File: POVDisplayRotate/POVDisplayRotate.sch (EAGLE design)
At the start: 34 parts, among them IC1 317EMP

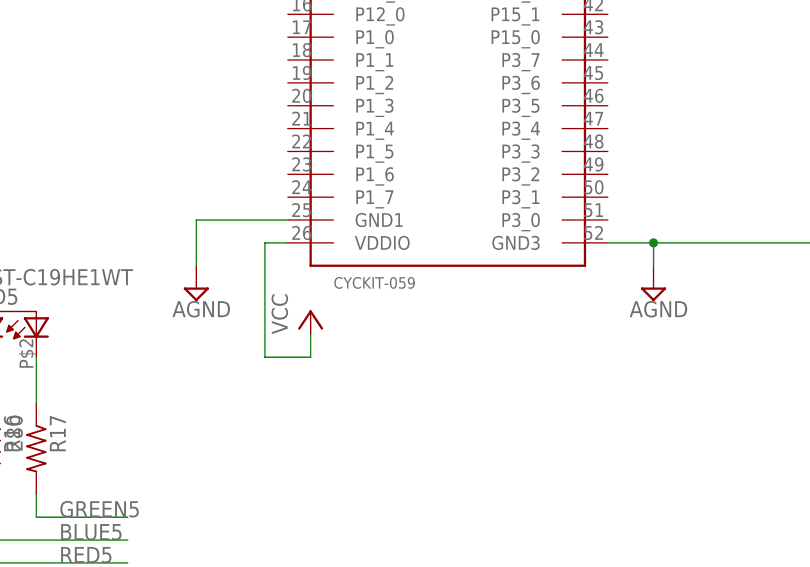
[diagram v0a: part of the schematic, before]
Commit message: Update the POVDisplayRotate.
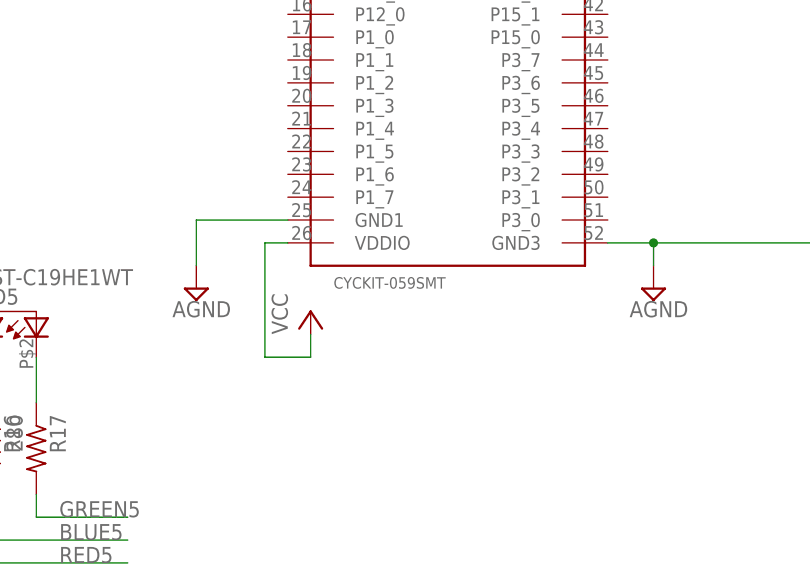
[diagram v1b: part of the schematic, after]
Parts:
- D2: DIGIKEY (none) -> 365-1908-1-ND
- U$1: value CYCKIT-059 -> CYCKIT-059SMT; device NicksParts:CYCKIT-059 -> NicksParts:CYCKIT-059SMT
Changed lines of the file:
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@@
 <grid distance="0.1" unitdist="inch" unit="inch" style="lines" multiple="1" display="no" altdistance="0.01" altunitdist="inch" altunit="inch"/>
 <layers>
-<layer number="1" name="Top" color="4" fill="1" visible="no" active="no"/>
-<layer number="16" name="Bottom" color="1" fill="1" visible="no" active="no"/>
-<layer number="17" name="Pads" color="2" fill="1" visible="no" active="no"/>
-<layer number="18" name="Vias" color="2" fill="1" visible="no" active="no"/>
-<layer number="19" name="Unrouted" color="6" fill="1" visible="no" active="no"/>
-<layer number="20" name="Dimension" color="15" fill="1" visible="no" active="no"/>
-<layer number="21" name="tPlace" color="7" fill="1" visible="no" active="no"/>
-<layer number="22" name="bPlace" color="7" fill="1" visible="no" active="no"/>
-<layer number="23" name="tOrigins" color="15" fill="1" visible="no" active="no"/>
-<layer number="24" name="bOrigins" color="15" fill="1" visible="no" active="no"/>
-<layer number="25" name="tNames" color="7" fill="1" visible="no" active="no"/>
-<layer number="26" name="bNames" color="7" fill="1" visible="no" active="no"/>
-<layer number="27" name="tValues" color="7" fill="1" visible="no" active="no"/>
-<layer number="28" name="bValues" color="7" fill="1" visible="no" active="no"/>
+<layer number="1" name="Top" color="4" fill="1" visible="yes" active="no"/>
+<layer number="16" name="Bottom" color="1" fill="1" visible="yes" active="no"/>
+<layer number="17" name="Pads" color="2" fill="1" visible="yes" active="no"/>
+<layer number="18" name="Vias" color="2" fill="1" visible="yes" active="no"/>
+<layer number="19" name="Unrouted" color="6" fill="1" visible="yes" active="no"/>
+<layer number="20" name="Dimension" color="15" fill="1" visible="yes" active="no"/>
+<layer number="21" name="tPlace" color="16" fill="1" visible="yes" active="no"/>
+<layer number="22" name="bPlace" color="14" fill="1" visible="yes" active="no"/>
+<layer number="23" name="tOrigins" color="15" fill="1" visible="yes" active="no"/>
+<layer number="24" name="bOrigins" color="15" fill="1" visible="yes" active="no"/>
+<layer number="25" name="tNames" color="7" fill="1" visible="yes" active="no"/>
+<layer number="26" name="bNames" color="7" fill="1" visible="yes" active="no"/>
+<layer number="27" name="tValues" color="7" fill="1" visible="yes" active="no"/>
+<layer number="28" name="bValues" color="7" fill="1" visible="yes" active="no"/>
 <layer number="29" name="tStop" color="7" fill="3" visible="no" active="no"/>
 <layer number="30" name="bStop" color="7" fill="6" visible="no" active="no"/>
@@
 <layer number="35" name="tGlue" color="7" fill="4" visible="no" active="no"/>
 <layer number="36" name="bGlue" color="7" fill="5" visible="no" active="no"/>
-<layer number="37" name="tTest" color="7" fill="1" visible="no" active="no"/>
-<layer number="38" name="bTest" color="7" fill="1" visible="no" active="no"/>
+<layer number="37" name="tTest" color="7" fill="1" visible="yes" active="no"/>
+<layer number="38" name="bTest" color="7" fill="1" visible="yes" active="no"/>
 <layer number="39" name="tKeepout" color="4" fill="11" visible="no" active="no"/>
 <layer number="40" name="bKeepout" color="1" fill="11" visible="no" active="no"/>
@@
 <layer number="44" name="Drills" color="7" fill="1" visible="no" active="no"/>
 <layer number="45" name="Holes" color="7" fill="1" visible="no" active="no"/>
-<layer number="46" name="Milling" color="3" fill="1" visible="no" active="no"/>
-<layer number="47" name="Measures" color="7" fill="1" visible="no" active="no"/>
-<layer number="48" name="Document" color="7" fill="1" visible="no" active="no"/>
-<layer number="49" name="Reference" color="7" fill="1" visible="no" active="no"/>
-<layer number="51" name="tDocu" color="6" fill="1" visible="no" active="no"/>
-<layer number="52" name="bDocu" color="7" fill="1" visible="no" active="no"/>
+<layer number="46" name="Milling" color="3" fill="1" visible="yes" active="no"/>
+<layer number="47" name="Measures" color="7" fill="1" visible="yes" active="no"/>
+<layer number="48" name="Document" color="7" fill="1" visible="yes" active="no"/>
+<layer number="49" name="Reference" color="7" fill="1" visible="yes" active="no"/>
+<layer number="51" name="tDocu" color="6" fill="1" visible="yes" active="no"/>
+<layer number="52" name="bDocu" color="7" fill="1" visible="yes" active="no"/>
 <layer number="90" name="Modules" color="5" fill="1" visible="yes" active="yes"/>
 <layer number="91" name="Nets" color="2" fill="1" visible="yes" active="yes"/>
@@
 <attribute name="DIGIKEY" value="MMSZ5232B-FDICT-ND"/>
 </part>
-<part name="U$1" library="NicksParts" deviceset="CY*CKIT-059" device=""/>
+<part name="U$1" library="NicksParts" deviceset="CY*CKIT-059" device="SMT" value="CYCKIT-059SMT"/>
 <part name="LED1" library="NicksParts" deviceset="LTST-C19HE1WT" device="">
 <attribute name="DIGIKEY" value="160-2162-1-ND"/>
@@
 <part name="SUPPLY10" library="supply2" deviceset="AGND" device=""/>
 <part name="P+4" library="supply1" deviceset="VCC" device=""/>
-<part name="D2" library="NicksParts" deviceset="OP980" device=""/>
+<part name="D2" library="NicksParts" deviceset="OP980" device="">
+<attribute name="DIGIKEY" value="365-1908-1-ND"/>
+</part>
 <part name="SUPPLY11" library="supply2" deviceset="AGND" device=""/>
 </parts>
@@
 <instance part="SUPPLY10" gate="G$1" x="231.14" y="27.94"/>
 <instance part="P+4" gate="VCC" x="193.04" y="25.4"/>
-<instance part="D2" gate="G$1" x="254" y="73.66"/>
+<instance part="D2" gate="G$1" x="254" y="73.66">
+<attribute name="DIGIKEY" x="254" y="73.66" size="1.778" layer="96" display="off"/>
+</instance>
 <instance part="SUPPLY11" gate="G$1" x="254" y="88.9"/>
 </instances>
@@
 </sheet>
 </sheets>
-<errors>
-</errors>
 </schematic>
 </drawing>

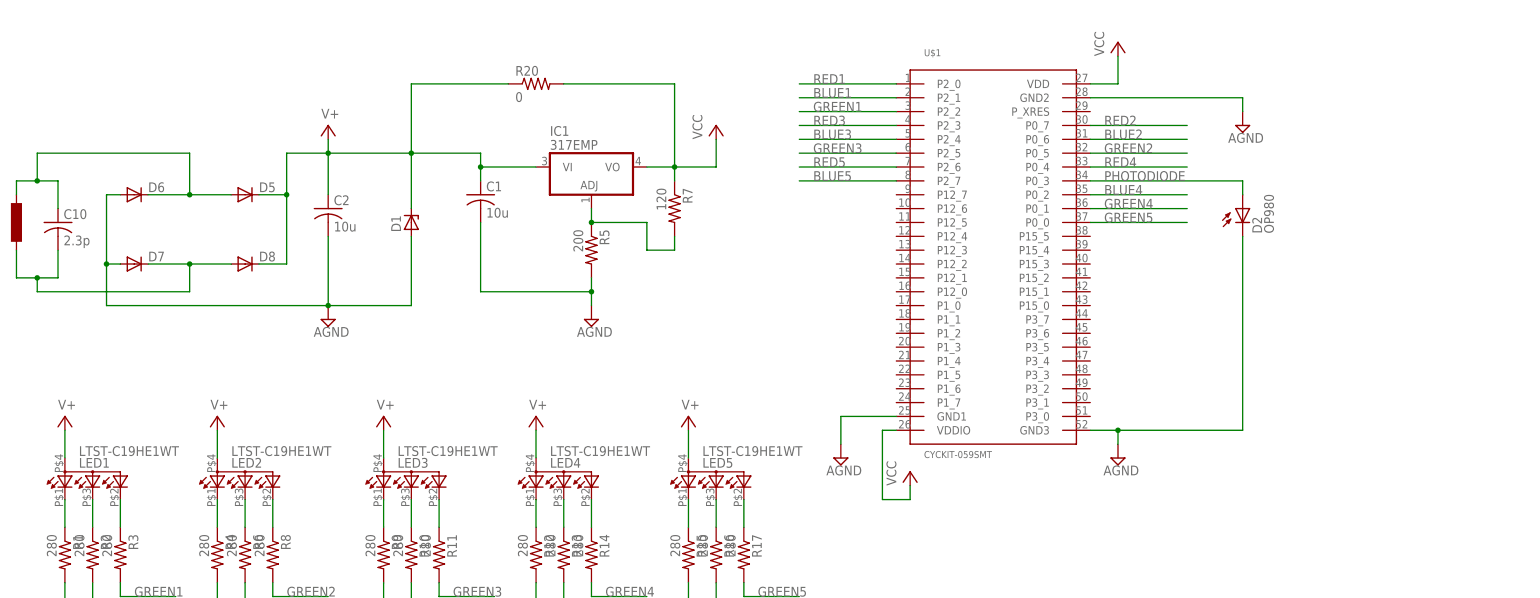
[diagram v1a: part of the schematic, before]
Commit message: Added Abercrombie blockage monitor.
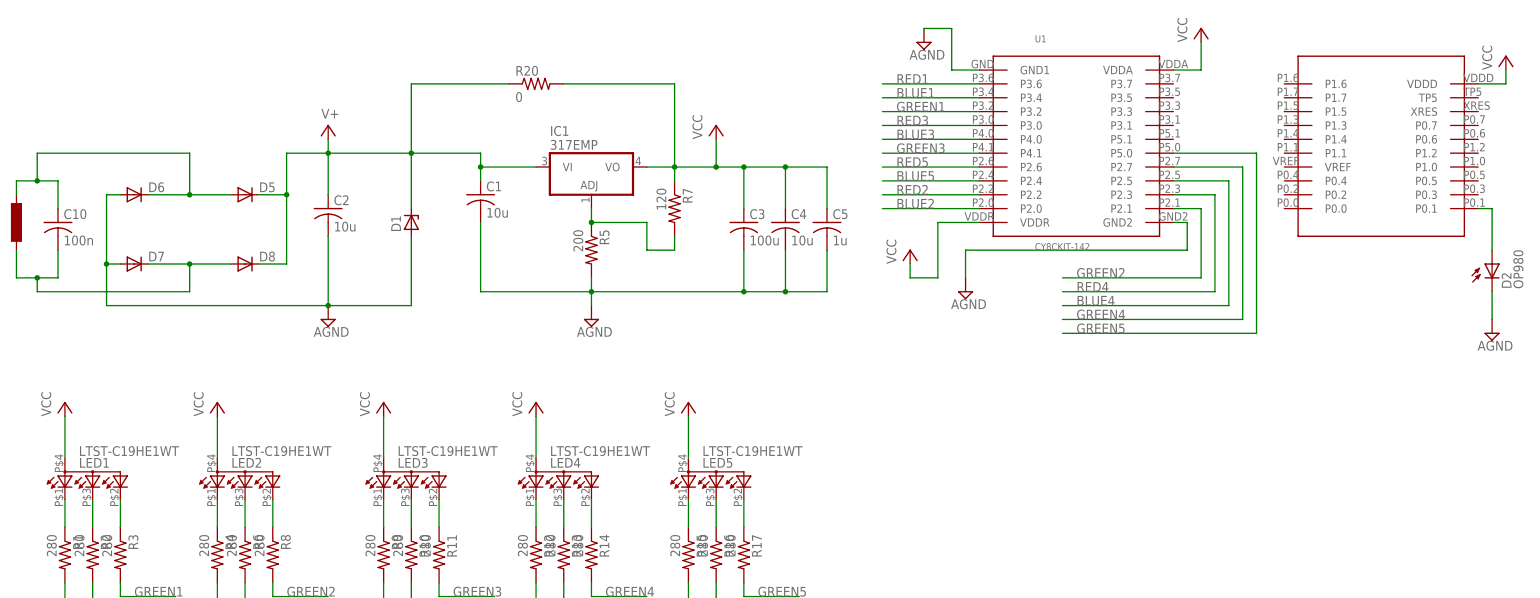
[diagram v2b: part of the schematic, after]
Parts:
- removed U$1: CYCKIT-059SMT, NicksParts:CYCKIT-059SMT
- added C3: 100u, resistor:C-USC0603
- added C4: 10u, resistor:C-USC0603
- added C5: 1u, resistor:C-USC0603
- added U1: CY8CKIT-142, NicksParts:CY8CKIT-142
- C10: value 2.3p -> 100n
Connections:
- net AGND: now also C3.2, C4.2, C5.2, U1.GND1, U1.GND2; no longer U$1.GND1, U$1.GND2, U$1.GND3
- net BLUE1: now also U1.P3.4; no longer U$1.P2_1
- net BLUE2: now also U1.P2.0; no longer U$1.P0_6
- net BLUE3: now also U1.P4.0; no longer U$1.P2_4
- net BLUE4: now also U1.P2.5; no longer U$1.P0_2
- net BLUE5: now also U1.P2.4; no longer U$1.P2_7
- net GREEN1: now also U1.P3.2; no longer U$1.P2_2
- net GREEN2: now also U1.P2.1; no longer U$1.P0_5
- net GREEN3: now also U1.P4.1; no longer U$1.P2_5
- net GREEN4: now also U1.P2.7; no longer U$1.P0_1
- net GREEN5: now also U1.P5.0; no longer U$1.P0_0
- net PHOTODIODE: now also U1.P0.1; no longer U$1.P0_3
- net RED1: now also U1.P3.6; no longer U$1.P2_0
- net RED2: now also U1.P2.2; no longer U$1.P0_7
- net RED3: now also U1.P3.0; no longer U$1.P2_3
- net RED4: now also U1.P2.3; no longer U$1.P0_4
- net RED5: now also U1.P2.6; no longer U$1.P2_6
- net V+: no longer LED1.A, LED2.A, LED3.A, LED4.A, LED5.A
- net VCC: now also C3.1, C4.1, C5.1, LED1.A, LED2.A, LED3.A, LED4.A, LED5.A, U1.VDDA, U1.VDDD, U1.VDDR; no longer U$1.VDD, U$1.VDDIO
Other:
- moved on the sheet: D2

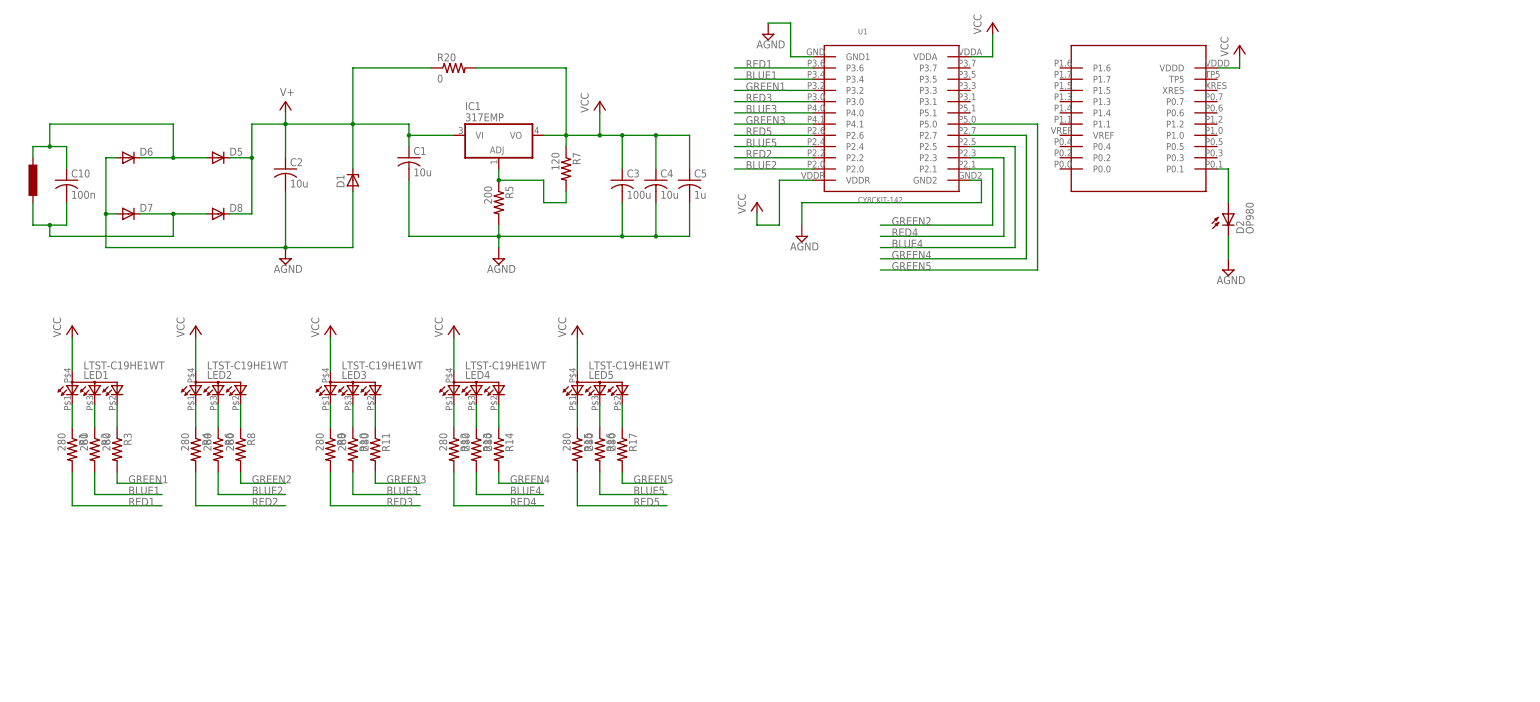
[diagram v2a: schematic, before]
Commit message: Updated the POVDisplayRotate
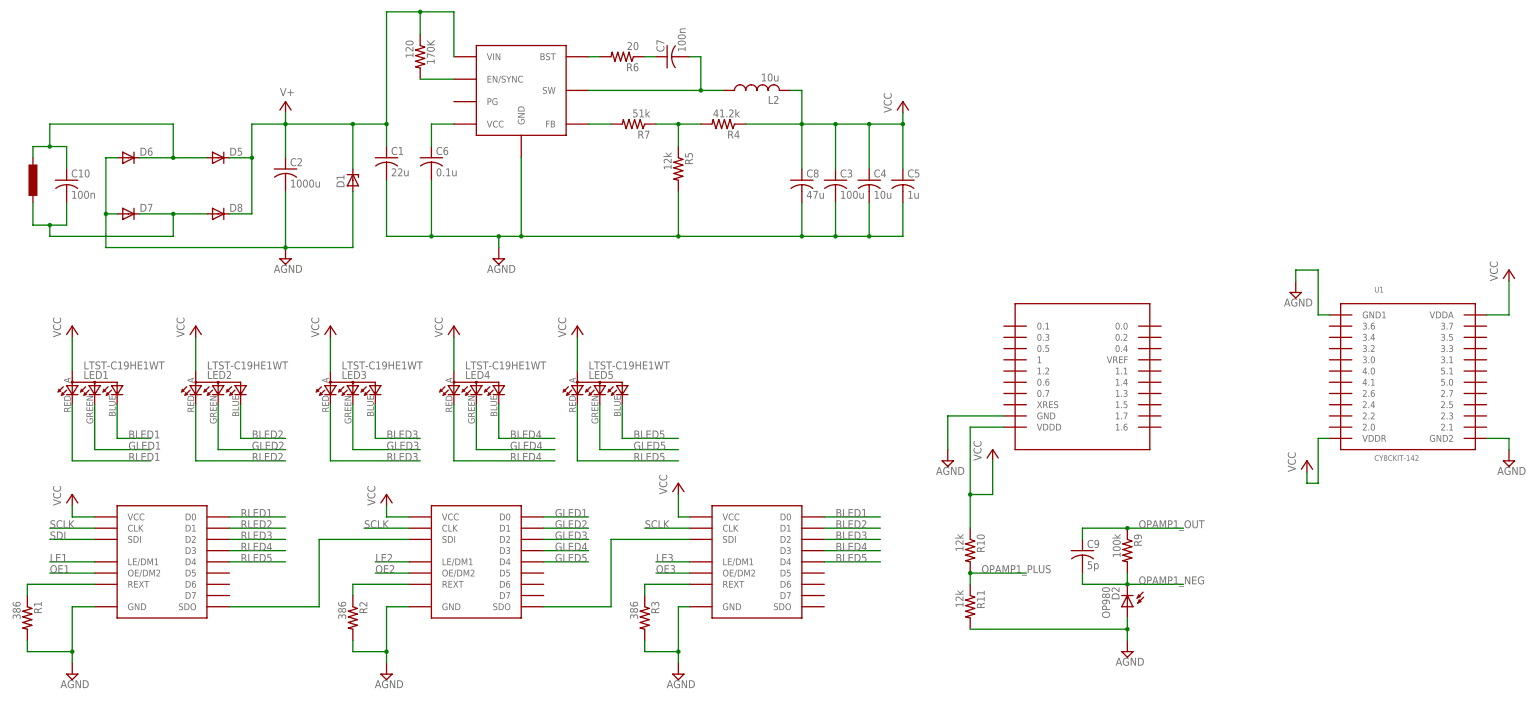
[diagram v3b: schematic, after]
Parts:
- removed IC1: 317EMP, linear:317EMP
- removed R12, R13, R14, R15, R16, R17, R8: 280, resistor:R-US_R0603
- removed R20: 0, resistor:R-US_R0603
- added 170K: 120, resistor:R-US_R0603
- added C6: 0.1u, resistor:C-USC0603
- added C7: 100n, resistor:C-USC0603
- added C8: 47u, resistor:C-USC0603
- added C9: 5p, resistor:C-USC0603
- added L2: 10u, resistor:L-USL1812
- added U2, U3, U4: STP08DP05, NicksParts:STP08DP05
- added U5: MPQ4420Q, NicksParts:MPQ4420Q
- C1: value 10u -> 22u
- C2: value 10u -> 1000u; device resistor:C-USC0603 -> resistor:C-USC1210
- C3: device resistor:C-USC0603 -> resistor:C-USC1210
- R1, R2, R3: value 280 -> 386
- R10, R11: value 280 -> 12k
- R4: value 280 -> 41.2k
- R5: value 200 -> 12k
- R6: value 280 -> 20
- R7: value 120 -> 51k
- R9: value 280 -> 100k
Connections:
- removed net BLUE1: R2.2, U1.P3.4
- removed net BLUE2: R6.2, U1.P2.0
- removed net BLUE3: R10.2, U1.P4.0
- removed net BLUE4: R13.2, U1.P2.5
- removed net BLUE5: R16.2, U1.P2.4
- removed net GREEN1: R3.2, U1.P3.2
- removed net GREEN2: R8.2, U1.P2.1
- removed net GREEN3: R11.2, U1.P4.1
- removed net GREEN4: R14.2, U1.P2.7
- removed net GREEN5: R17.2, U1.P5.0
- removed net N$13: LED4.CRED, R12.1
- removed net N$14: LED4.CBLUE, R13.1
- removed net N$15: LED4.CGREEN, R14.1
- removed net N$16: LED5.CRED, R15.1
- removed net N$17: LED5.CBLUE, R16.1
- removed net N$3: LED1.CBLUE, R2.1
- removed net PHOTODIODE: D2.A, U1.P0.1
- removed net RED1: R1.2, U1.P3.6
- removed net RED2: R4.2, U1.P2.2
- removed net RED3: R9.2, U1.P3.0
- removed net RED4: R12.2, U1.P2.3
- removed net RED5: R15.2, U1.P2.6
- new net BLED1: LED1.CBLUE, U4.D0
- new net BLED2: LED2.CBLUE, U4.D1
- new net BLED3: LED3.CBLUE, U4.D2
- new net BLED4: LED4.CBLUE, U4.D3
- new net BLED5: LED5.CBLUE, U4.D4
- new net GLED1: LED1.CGREEN, U3.D0
- new net GLED2: LED2.CGREEN, U3.D1
- new net GLED3: LED3.CGREEN, U3.D2
- new net GLED4: LED4.CGREEN, U3.D3
- new net GLED5: LED5.CGREEN, U3.D4
- new net LE1: U2.LE/DM1
- new net LE2: U3.LE/DM1
- new net LE3: U4.LE/DM1
- new net N$1: C6.1, U5.VCC
- new net N$8: C7.1, R6.1
- new net OE1: U2.OE/DM2
- new net OE2: U3.OE/DM2
- new net OE3: U4.OE/DM2
- new net OPAMP1_NEG: C9.2, D2.C, R9.2
- new net OPAMP1_OUT: C9.1, R9.1
- new net OPAMP1_PLUS: R10.2, R11.1
- new net RLED1: LED1.CRED, U2.D0
- new net RLED2: LED2.CRED, U2.D1
- new net RLED3: LED3.CRED, U2.D2
- new net RLED4: LED4.CRED, U2.D3
- new net RLED5: LED5.CRED, U2.D4
- new net SCLK: U2.CLK, U3.CLK, U4.CLK
- new net SDI: U2.SDI
- net AGND: now also C6.2, C8.2, D2.A, R1.2, R11.2, R2.2, R3.2, U1.GND, U2.GND, U3.GND, U4.GND, U5.GND; no longer D2.C
- net N$10: now also R2.1, U3.REXT; no longer LED3.CRED, R9.1
- net N$11: now also U3.SDO, U4.SDI; no longer LED3.CBLUE, R10.1
- net N$12: now also R3.1, U4.REXT; no longer LED3.CGREEN, R11.1
- net N$18: now also U2.SDO, U3.SDI; no longer LED5.CGREEN, R17.1
- net N$2: now also 170K.2, U5.EN/SYNC; no longer LED1.CRED, R1.1
- net N$4: now also R7.2, U5.FB; no longer LED1.CGREEN, R3.1
- net N$5: now also R4.2, R5.1, R7.1; no longer LED2.CRED, R4.1
- net N$6: now also R1.1, U2.REXT; no longer LED2.CBLUE, R6.1
- net N$7: now also R6.2, U5.BST; no longer IC1.ADJ, R5.1, R7.2
- net N$9: now also C7.2, L2.1, U5.SW; no longer LED2.CGREEN, R8.1
- net V+: now also 170K.1, U5.VIN; no longer IC1.VI, R20.1
- net VCC: now also C8.1, L2.2, R10.1, R4.1, U2.VCC, U3.VCC, U4.VCC; no longer IC1.VO, R20.2, R7.1
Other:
- moved on the sheet: C1, C3, C4, C5, D2, LED1, LED2, LED3, LED4, LED5, R1, R10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
